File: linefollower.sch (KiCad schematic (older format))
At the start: 118 parts, among them J1 BATT, J10 I2C, J11 BT_module, J12 USB_B_Micro, J13 Conn_02x20_Odd_Even, J14 Micro_SD_Card_Det, J15 Conn_linesens_Female, J16 Conn_linesens_Male, J2 3v3, J21 ESC_MOTOR, J22 MOTOR_ESC, J3 3v3, J4 5v, J5 SWD+UART, J6 SPI2, J7 I2C, J8 ESC, J9 ESC_CTRL, SW1 uBTN_0, SW2 uBTN_1, SW3 uBTN_2, SW4 uBTN_3, SW5 SW_DIP_x04, SW6 RST, U1 ACS712xLCTR-30A, U10 Troyka-IMU10, U11 AltIMU-10v5, U12 UM7, U13 STM32F429ZITx, U2 L7805, U3 LM1117-3.3, U4 IP4220CZ6, U5 MAX14870_carrier, U6 MAX14870_carrier, U7 ADG726BSUZ, U8 M_R, U9 M_L, Y1 8MHz, Y2 32MHz

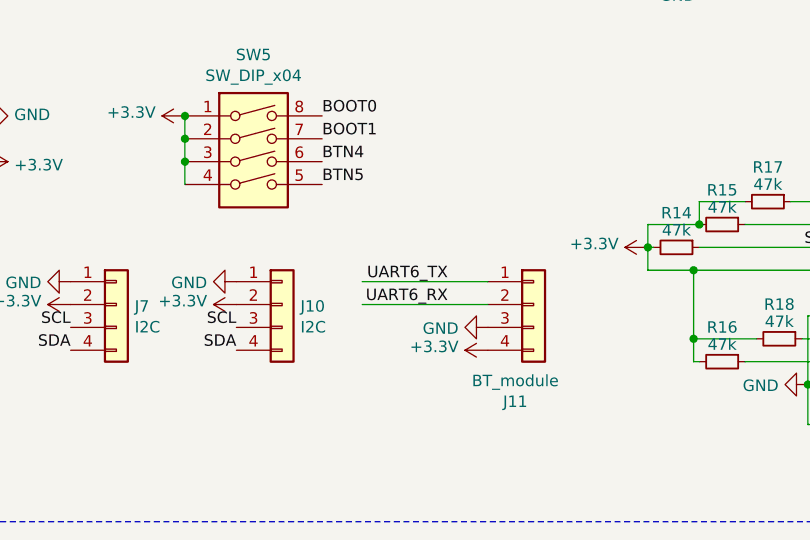
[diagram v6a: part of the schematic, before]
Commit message: All PCB components places
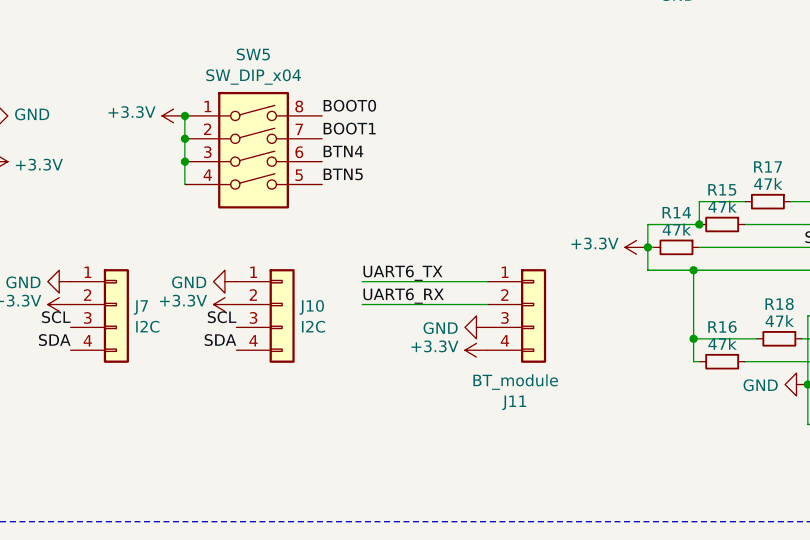
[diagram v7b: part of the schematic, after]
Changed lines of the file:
@@
 	0    1    1    0
 $EndComp
-Text Label 5525 10150 2    50   ~ 0
+Text Label 5150 10150 0    50   ~ 0
 UART6_RX
-Text Label 5525 10050 2    50   ~ 0
+Text Label 5150 10050 0    50   ~ 0
 UART6_TX
 Wire Wire Line

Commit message: Finished connection of PCBs
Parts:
- J16: footprint Connector_PinSocket_2.54mm:PinSocket_1x11_P2.54mm_Horizontal -> linefollower:SolderedPad_1x11_P2.54
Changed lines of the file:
@@
 F 0 "J16" H 5175 2525 50  0000 C CNN
 F 1 "Conn_linesens_Male" H 5475 2425 50  0000 C CNN
-F 2 "Connector_PinSocket_2.54mm:PinSocket_1x11_P2.54mm_Horizontal" H 5150 1800 50  0001 C CNN
+F 2 "linefollower:SolderedPad_1x11_P2.54" H 5150 1800 50  0001 C CNN
 F 3 "~" H 5150 1800 50  0001 C CNN
 	1    5150 1800
